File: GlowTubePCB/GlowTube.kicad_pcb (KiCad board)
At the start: 2 copper layers, 80.7 x 94.8 mm, 39 parts, among them J1 Conn_01x07, P1 Solder_Pad, P2 Solder_Pad, P3 Solder_Pad, P4 Solder_Pad, P5 Solder_Pad, P6 Solder_Pad, SW1 TS-1185EC-C-D-B, SW2 TS-1185EC-C-D-B, U1 SN74AHCT32QPWRQ1, U2 ESP32-WROOM-32E (4MB), U3 CP2102-GMR, U4 BL1117-33CX, U5 UMH3N, U6 GMA4030H11-F26

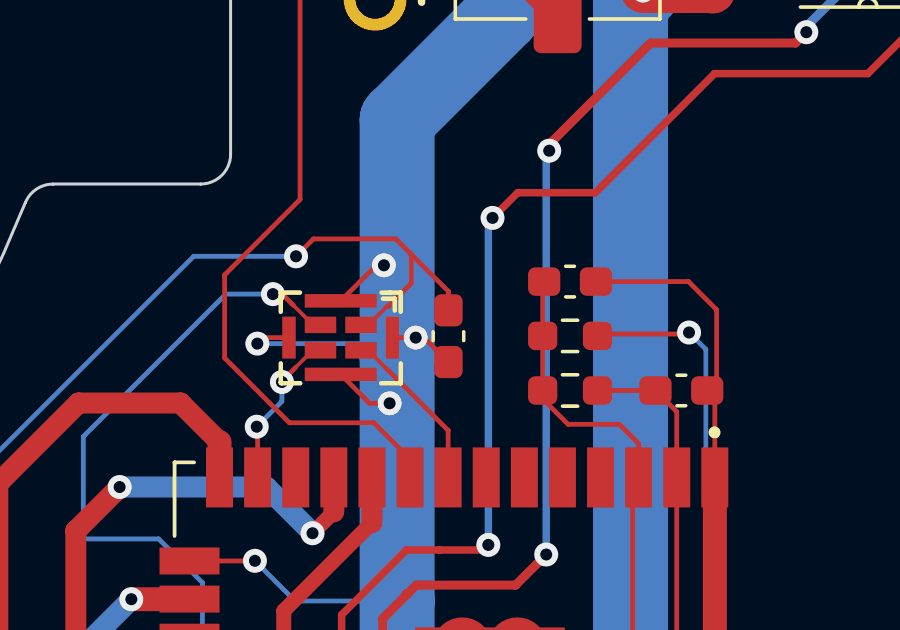
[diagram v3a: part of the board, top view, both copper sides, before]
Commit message: added temp wall mount and updated mic
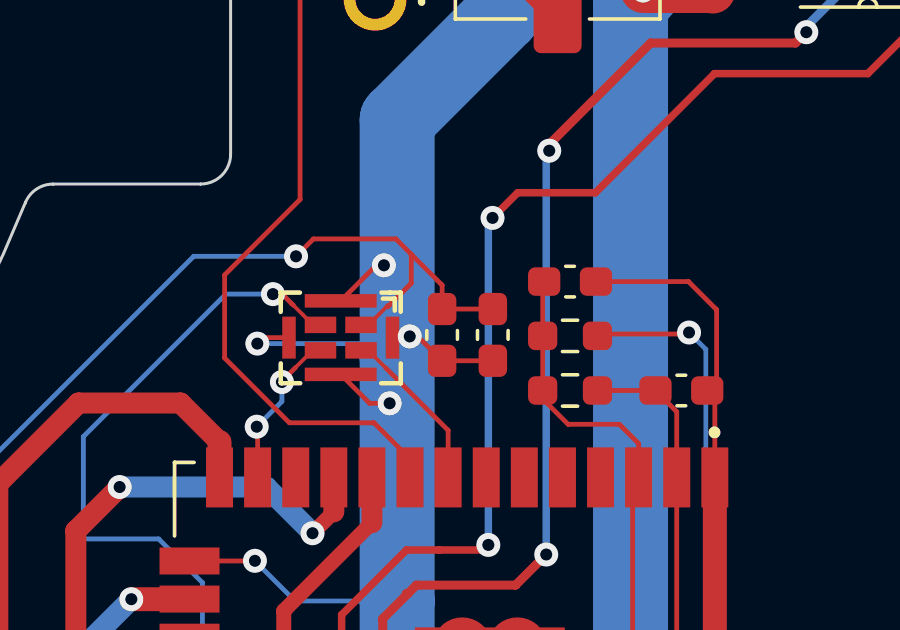
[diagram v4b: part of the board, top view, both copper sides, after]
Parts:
- added C13: 10uF, Capacitor_SMD:C_0603_1608Metric_Pad1.08x0.95mm_HandSolder, F.Cu at (142.3, 105.8)
- U6: value GMA4030H11-F26 -> MSM261D4030H1CPM; footprint GMA4030H11-F26:GMA4030H11-F26 -> footprint:MIC-SMD_8P-L3.0-W4.0-P0.85-BL
- moved C9 0.21 mm to (140.6, 105.8)
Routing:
- net GND: track 354.9 -> 356.6 mm
- net +3V3: track 173.4 -> 174.9 mm

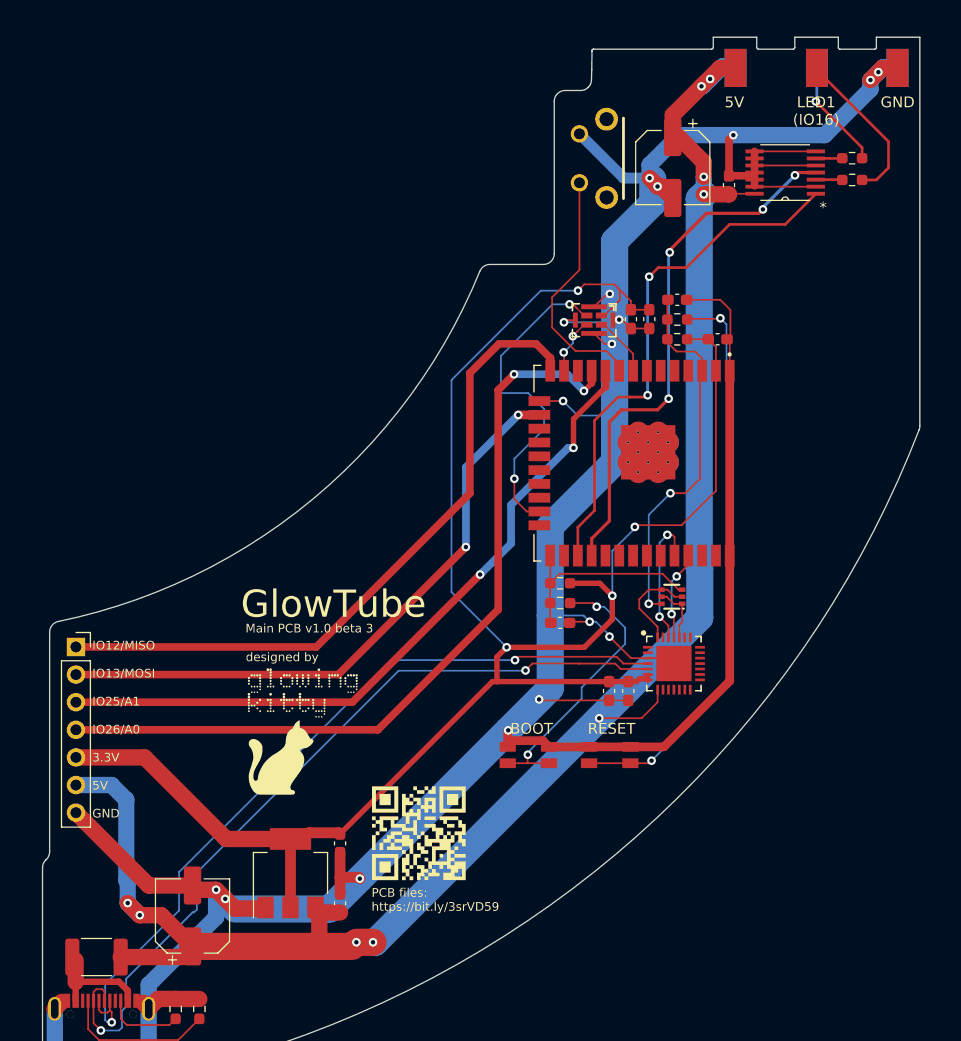
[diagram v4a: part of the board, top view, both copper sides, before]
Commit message: replaced microphone and levelshifter
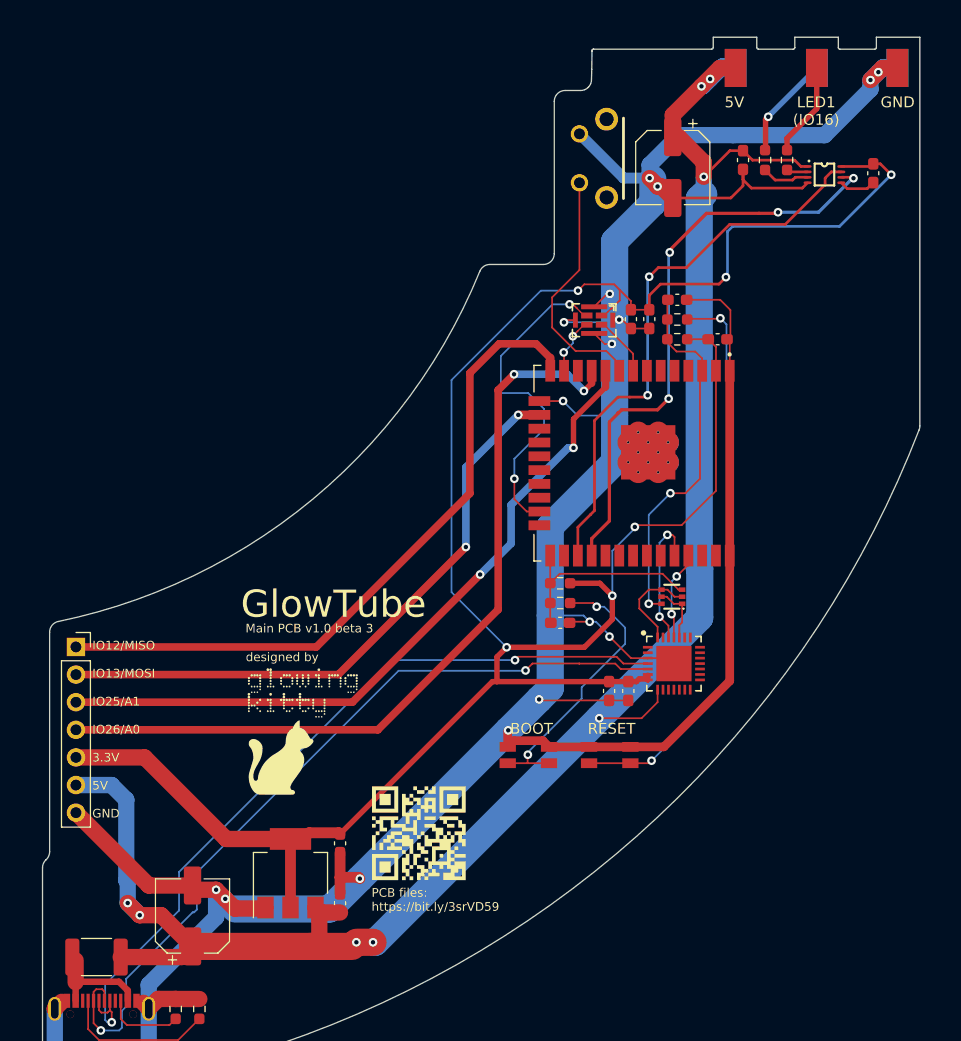
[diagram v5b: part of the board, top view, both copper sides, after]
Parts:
- added C14: 0.1uF, Capacitor_SMD:C_0603_1608Metric_Pad1.08x0.95mm_HandSolder, F.Cu at (162.9, 92.4)
- U1: value SN74AHCT32QPWRQ1 -> SN74LVC2T45DCUR; footprint SN74AHCT32QPWRQ1:SN74AHCT32QPWRQ1 -> footprint:VSSOP-8_L2.4-W2.1-P0.50-LS3.2-BR
- moved R8 8.02 mm to (152.9, 91.2), turned to 90 degrees
- moved R1 6.26 mm to (154.9, 91.2), turned to 90 degrees
- moved U1 3.61 mm to (158.4, 92.5)
- moved C2 2.64 mm to (150.9, 91.2), turned to -90 degrees
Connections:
- U1 pad 1: IO16/LED1 -> +5V
- U1 pad 2: GND -> Net-(R1-Pad1)
- U1 pad 3: Net-(R1-Pad1) -> Net-(R8-Pad1)
- U1 pad 4: IO17/LED2 -> GND
- U1 pad 6: Net-(R8-Pad1) -> IO17/LED2
- U1 pad 7: GND -> IO16/LED1
- U1 pad 8: GND -> +3V3
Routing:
- net +3V3: track 174.9 -> 210.6 mm, vias 4 -> 6
- net GND: track 356.6 -> 348.8 mm, vias 17 -> 16
- net +5V: track 167.9 -> 174.4 mm, vias 9 -> 8
- net LED1 DATA OUT: track 14.8 -> 8.87 mm
- net IO17/LED2: track 49.6 -> 53.9 mm
- net IO16/LED1: track 48.4 -> 51.9 mm
- net Net-(R8-Pad1): track 2.44 -> 4.41 mm
- net LED2 DATA OUT: track 10.1 -> 9.53 mm

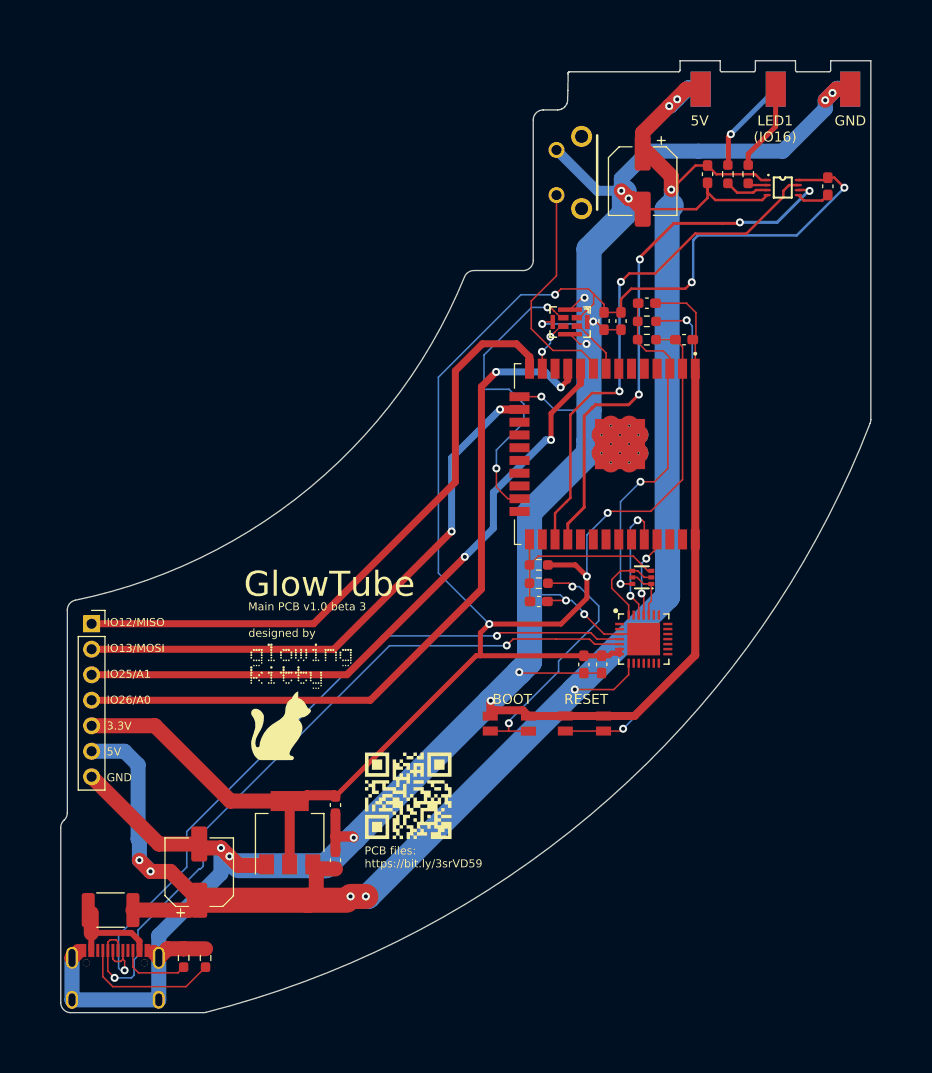
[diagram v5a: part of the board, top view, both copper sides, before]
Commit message: updated PCB designs to release candidate 1
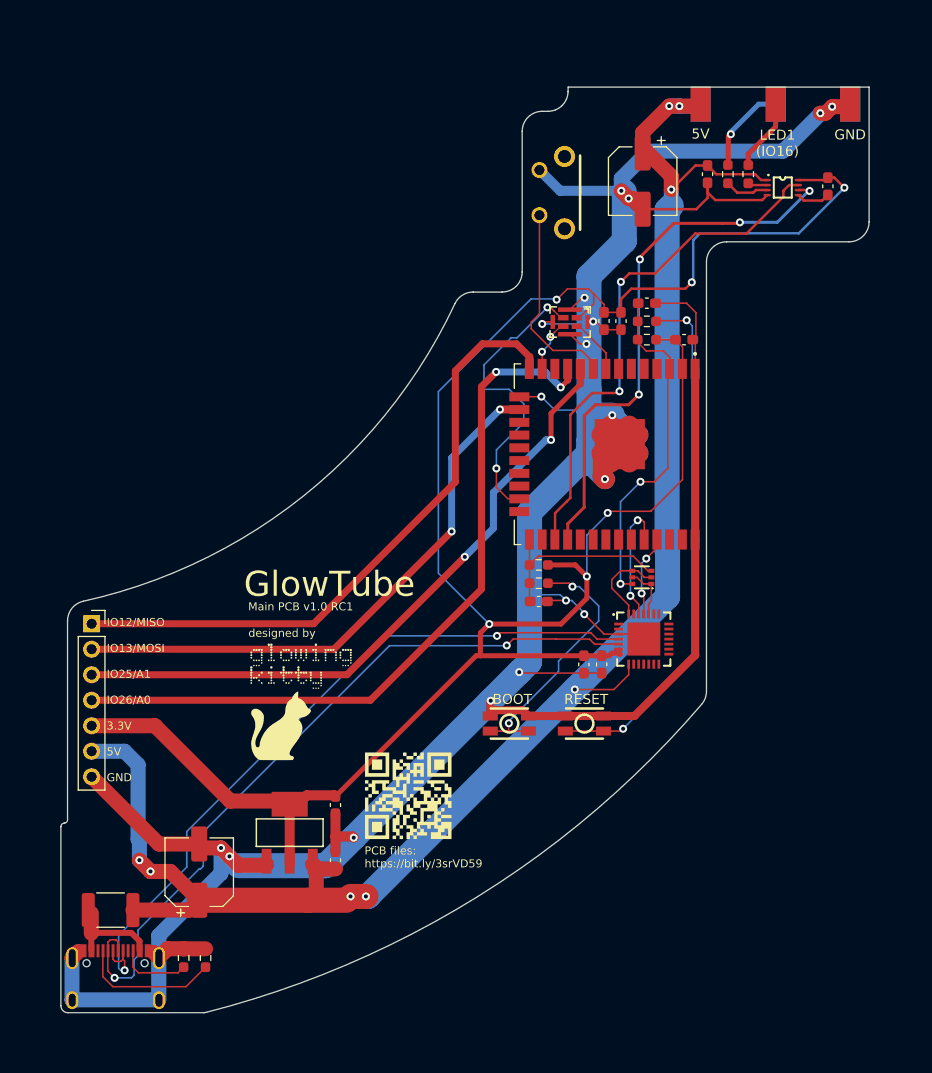
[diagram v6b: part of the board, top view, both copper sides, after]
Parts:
- SW1, SW2: footprint TS-1185EC-C-D-B:TS-1185EC-C-D-B -> footprint:SW-SMD_4P-L3.7-W3.0-P1.50-LS4.7
- U2: value ESP32-WROOM-32E (4MB) -> ESP32-WROOM-32E; footprint ESP32-WROOM-32E__16MB_:MODULE_ESP32-WROOM-32E_(16MB) -> footprint:WIFI-SMD_ESP32-WROOM-32E
- U3: footprint CP2102-GMR:CP2102-GMR -> footprint:QFN-28_L5.0-W5.0-P0.50-BL-EP
- U4: footprint Package_TO_SOT_SMD:SOT-223 -> footprint:SOT-223-4_L6.5-W3.5-P2.30-LS7.0-BR
- USB1: value U262-16XN-4BVC11 -> U262-161N-4BVC11; footprint U262-161N-4BVC11:USB-3.1-SMD_U262-161N-4BVC11 -> footprint:USB-3.1-SMD_U262-161N-4BVC11
- moved C12 2.62 mm to (133.2, 93.0)
- moved P2 1.50 mm to (157.8, 84.2)
- moved P3 1.50 mm to (165.2, 84.2)
- moved P4 1.50 mm to (150.1, 84.2)
- moved P5 1.50 mm to (165.0, 84.2)
- moved P6 1.50 mm to (157.6, 84.2)
- moved U2 1.20 mm to (143.5, 118.3)
- moved USB1 1.20 mm to (91.8, 172.2)
- moved P1 0.90 mm to (150.3, 83.6)
- turned U3 to -90 degrees
- turned U4 to -90 degrees
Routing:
- net GND: track 348.8 -> 356.1 mm, vias 16 -> 18
- net IO33/MAINBUTTON: track 22.5 -> 19.8 mm
- net +5V: track 174.4 -> 173.0 mm
- net +3V3: track 210.6 -> 209.8 mm
- net IO15/WS: track 30.6 -> 30.0 mm
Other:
- board size 80.7 x 94.8 mm -> 80.5 x 92.2 mm
- board text added: "Main PCB v1.0 RC1"
- board text removed: "Main PCB v1.0 beta 3"

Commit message: fixed pcbs
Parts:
- added OSHW logo: OSHW-Logo2_7.3x6mm_SilkScreen, Symbol:OSHW-Logo2_7.3x6mm_SilkScreen, F.Cu at (108.2, 166.4)

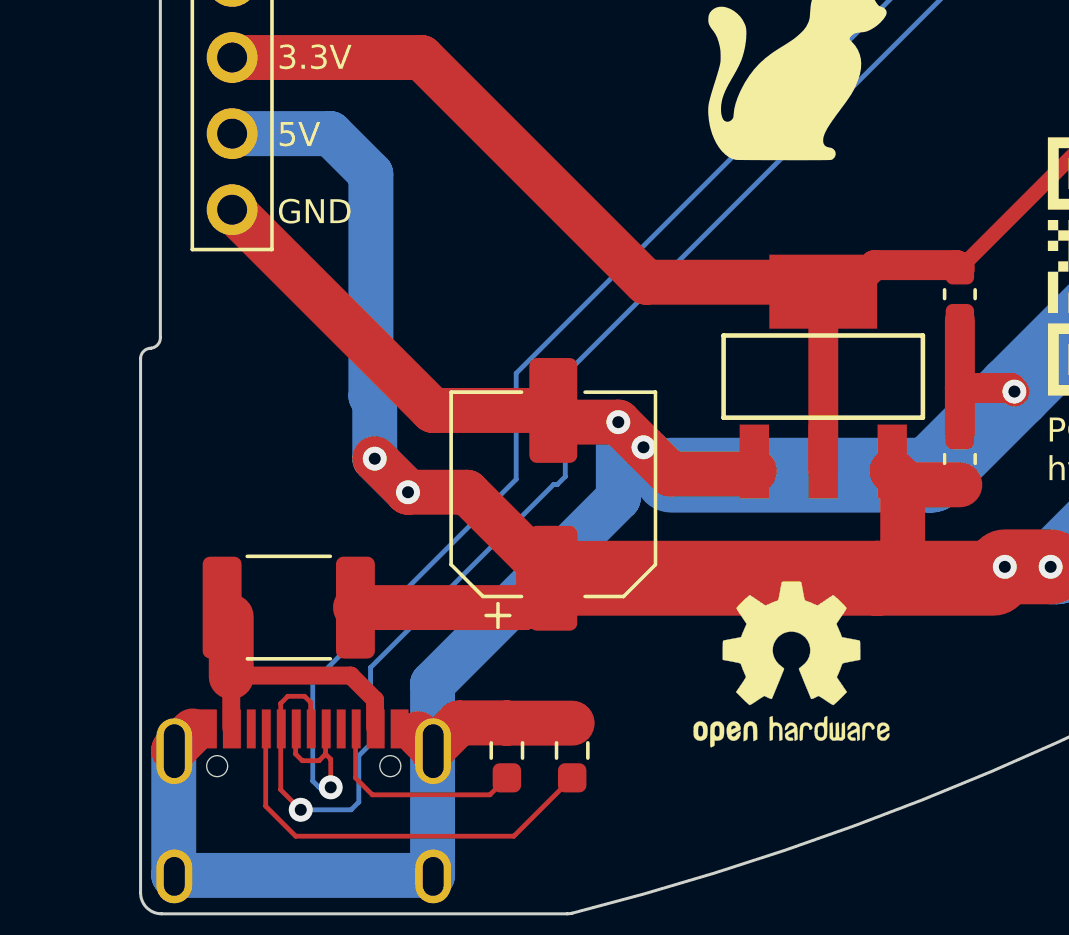
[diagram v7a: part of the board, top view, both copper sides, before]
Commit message: added schottky diode to protect usb-c port
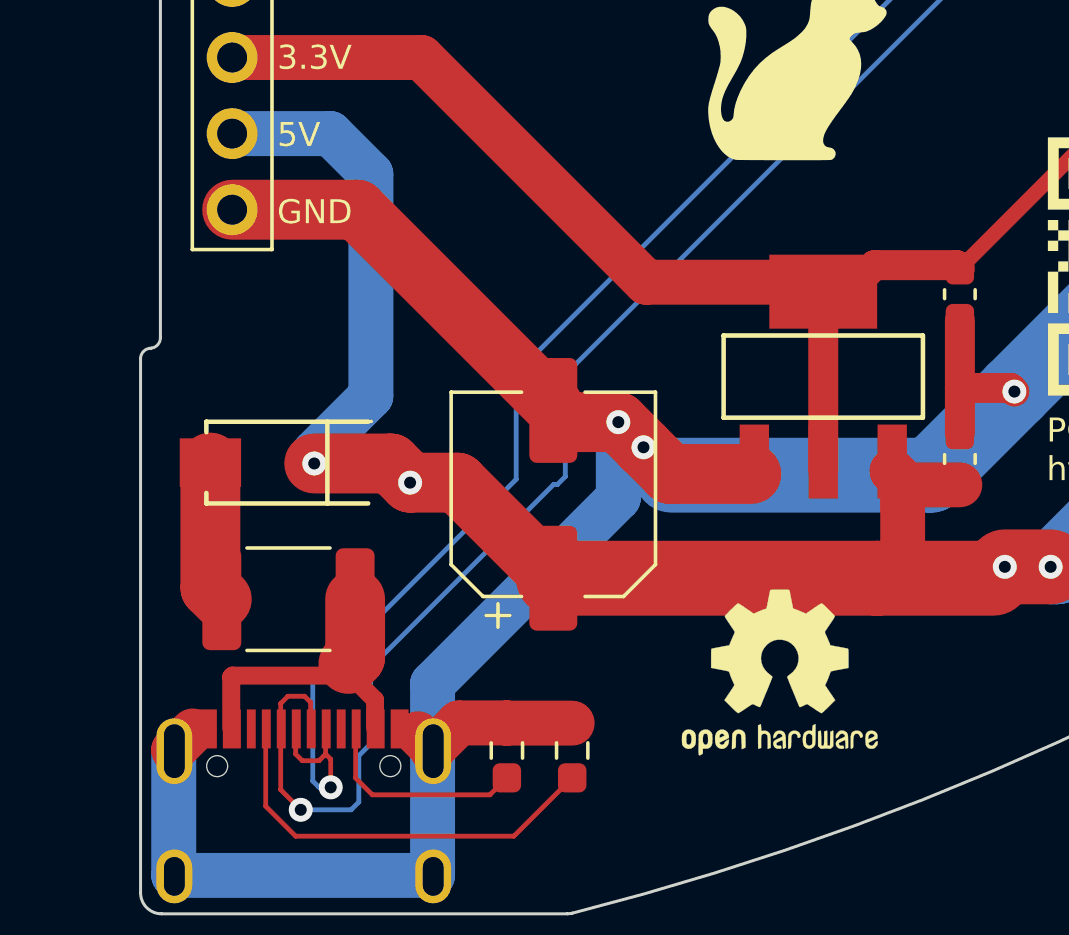
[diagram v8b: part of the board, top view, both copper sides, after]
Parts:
- added U7: SS54, footprint:SMA_L4.4-W2.8-LS5.4-RD, F.Cu at (91.4, 159.6)
- moved OSHW logo 0.47 mm to (107.8, 166.6)
- moved F1 0.28 mm to (91.4, 164.2), turned to 180 degrees
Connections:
- F1 pad 2: +5V -> Net-(F1-Pad2)
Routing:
- net Net-(F1-Pad2): track 0.00 -> 5.15 mm
- net +5V: track 173.0 -> 170.7 mm
